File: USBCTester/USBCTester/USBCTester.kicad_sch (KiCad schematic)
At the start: 93 parts, among them J1 USB4080-03-A, J2 USB4080-03-A, J3 Conn_01x14, J4 Conn_01x03, J6 Conn_01x03, SW1 SW_Push, U1 74HC595, U2 74HC595, U3 74HC595, U4 74HC595, U5 74HC595, U6 74HC595, U7 RaspberryPi_Pico

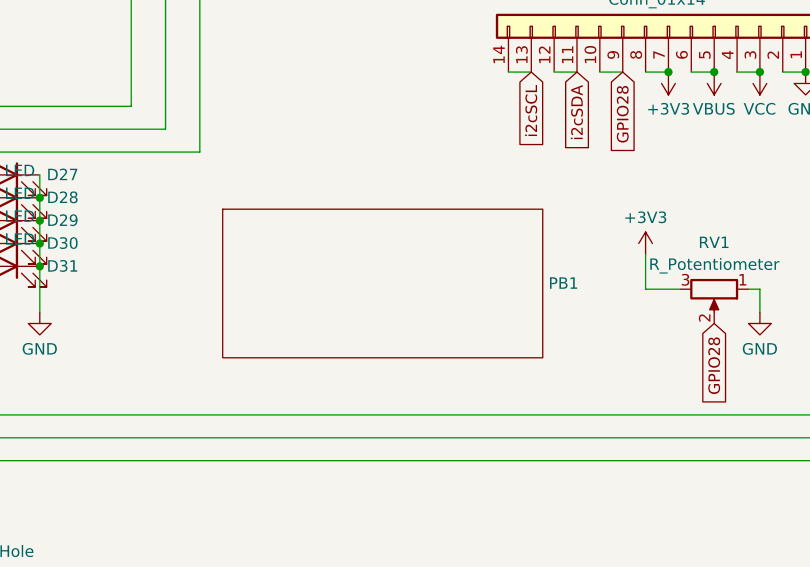
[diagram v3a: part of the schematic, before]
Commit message: use older footprint for USBC since JLCPCB does seem to tolerate the shape, and minor silkscreen fixes
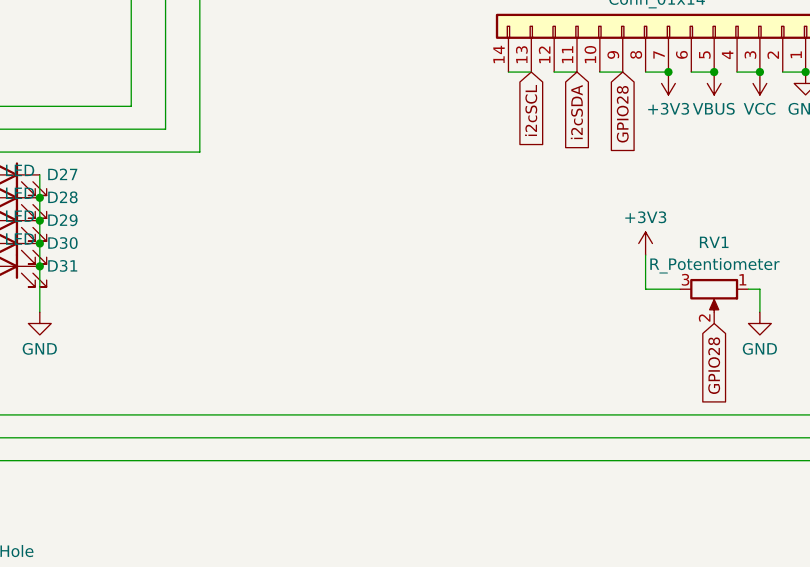
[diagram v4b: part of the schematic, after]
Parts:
- removed PB1: ~, ProtoBoard:ProtoBoard 14x6, symbol ProtoBoard:14x6ProtoBoard
